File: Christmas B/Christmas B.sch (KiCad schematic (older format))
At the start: 20 parts, among them J1 LEFT, J2 RIGHT

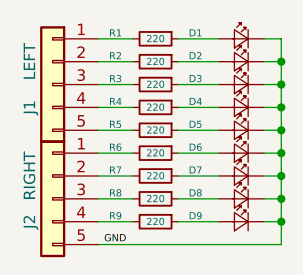
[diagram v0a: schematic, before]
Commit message: Added B side
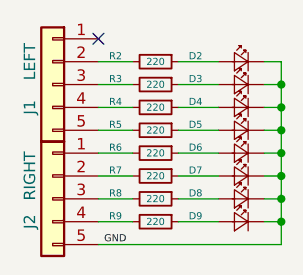
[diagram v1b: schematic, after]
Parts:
- removed D1: LED_Small, christmas:top_star, symbol Device:LED_Small
- removed R1: 220, christmas:resistor, symbol Device:R_Small
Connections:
- no-connect marks 0 -> 1
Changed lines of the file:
@@
 encoding utf-8
 Sheet 1 1
-Title "Christmas A"
+Title "Christmas B"
 Date ""
 Rev "A"
 Comp ""
-Comment1 "A-side of the christmas tree."
-Comment2 "Slot into B-side before soldering star into place."
-Comment3 ""
-Comment4 ""
+Comment1 ""
+Comment2 ""
+Comment3 "Slot into A-side before soldering star into place."
+Comment4 "B-side of the christmas tree."
 $EndDescr
-$Comp
-L Device:R_Small R1
-U 1 1 5F863E92
-P 3950 2450
-F 0 "R1" V 3925 2275 31  0000 C CNN
-F 1 "220" V 3950 2450 31  0000 C CNN
-F 2 "christmas:resistor" H 3950 2450 50  0001 C CNN
-F 3 "~" H 3950 2450 50  0001 C CNN
-	1    3950 2450
-	0    1    1    0
-$EndComp
-Wire Wire Line
-	3700 2450 3850 2450
 $Comp
 L Device:R_Small R2
@@
 	4050 3250 4225 3250
 Wire Wire Line
-	4500 2450 4500 2550
-Wire Wire Line
 	4500 3250 4425 3250
 Wire Wire Line
@@
 Wire Wire Line
 	4425 2550 4500 2550
-Connection ~ 4500 2550
 Wire Wire Line
 	4500 2550 4500 2650
@@
 	-1   0    0    -1
 $EndComp
-$Comp
-L Device:LED_Small D1
-U 1 1 5F89482E
-P 4325 2450
-F 0 "D1" H 4525 2475 31  0000 C CNN
-F 1 "LED_Small" H 4325 2336 50  0001 C CNN
-F 2 "christmas:top_star" V 4325 2450 50  0001 C CNN
-F 3 "~" V 4325 2450 50  0001 C CNN
-	1    4325 2450
-	-1   0    0    -1
-$EndComp
-Wire Wire Line
-	4050 2450 4225 2450
-Wire Wire Line
-	4425 2450 4500 2450
+NoConn ~ 3700 2450
 $EndSCHEMATC
